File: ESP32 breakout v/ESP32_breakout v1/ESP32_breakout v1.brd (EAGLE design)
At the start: 50.8 x 50.8 mm, 18 parts, among them U1 ESP-WROOM-32, U2 AP7361C-33E-13

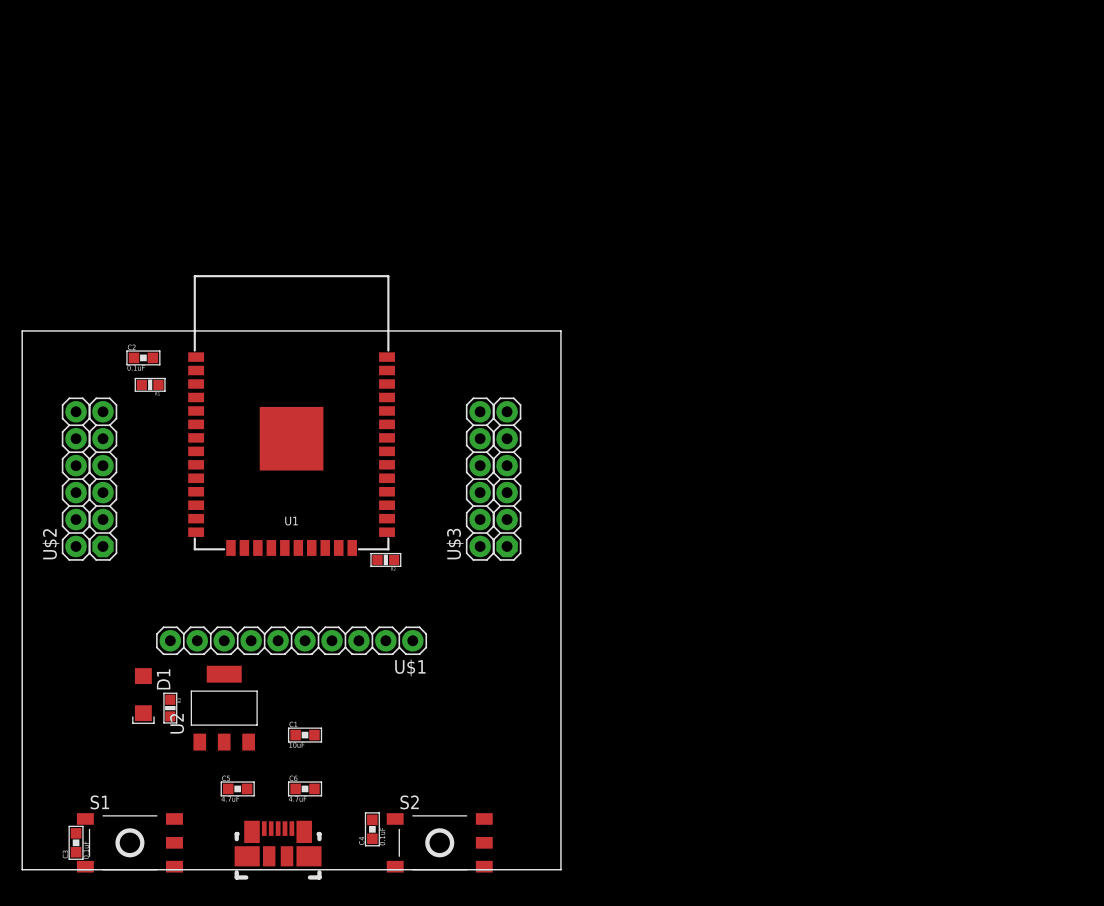
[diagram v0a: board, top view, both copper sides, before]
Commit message: Added USB ccomponents
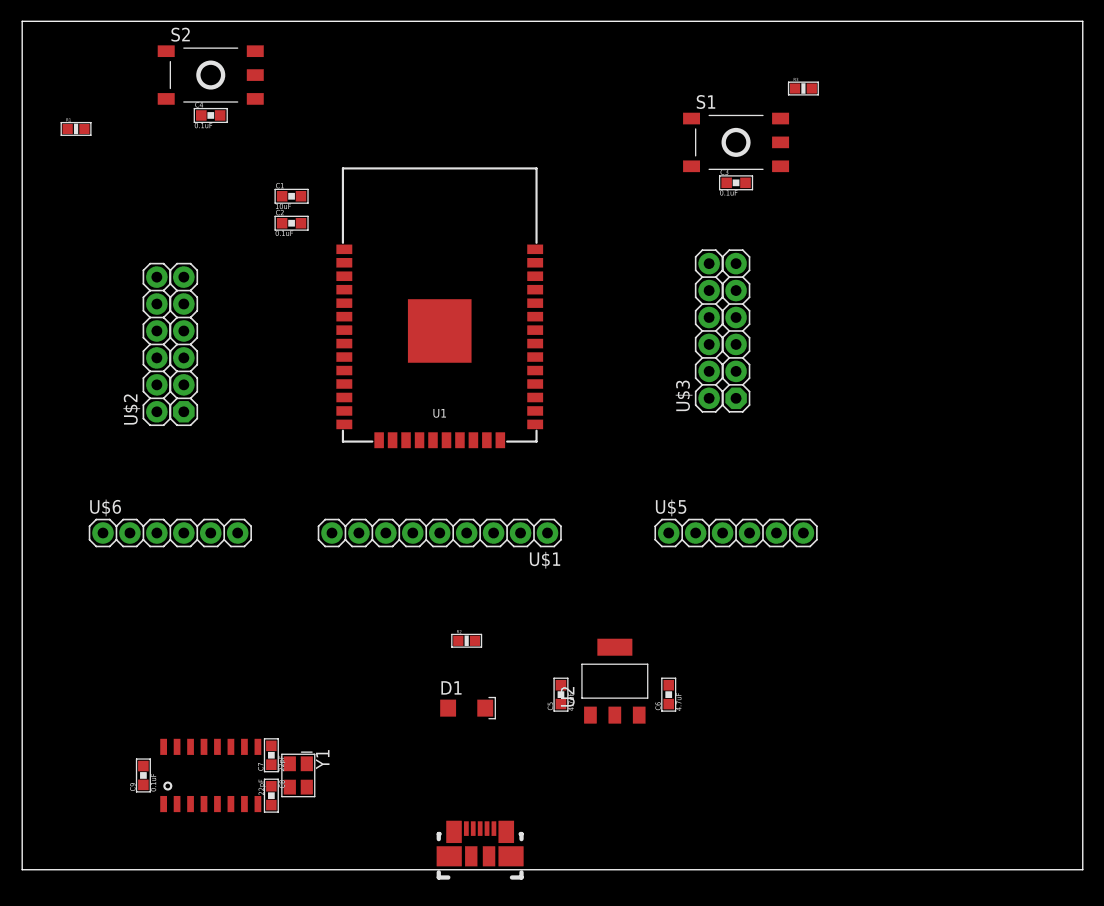
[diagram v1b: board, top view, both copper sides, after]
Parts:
- added C7, C8: 22pF, dr-library:CAP-0603
- added C9: 0.1uF, dr-library:CAP-0603
- added U$5, U$6: M06, dr-library:1X06
- added U$7: CH340G, usb-serial:SOIC16
- added Y1: (no value), dr-library:CFPX-180
- U$1: value M10 -> M09; device dr-library:1X10 -> dr-library:1X09
- moved C3 88.0 mm to (67.3, 64.8), turned to 0 degrees
- moved S1 87.3 mm to (67.3, 68.6)
- moved R3 83.5 mm to (73.7, 73.7), turned to 0 degrees
- moved S2 75.5 mm to (17.8, 74.9)
- moved C4 69.0 mm to (17.8, 71.1), turned to 0 degrees
- moved C1 50.8 mm to (25.4, 63.5)
- moved U2 36.9 mm to (55.9, 17.8)
- moved C6 35.4 mm to (61.0, 16.5), turned to 90 degrees
- moved C5 31.8 mm to (50.8, 16.5), turned to 90 degrees
- moved D1 30.5 mm to (41.9, 15.2), turned to 0 degrees
- moved U$3 25.7 mm to (64.8, 45.7)
- moved R1 25.1 mm to (5.08, 69.8), turned to 0 degrees
- moved U$4 19.1 mm to (43.2, 1.27)
- moved C2 18.9 mm to (25.4, 61.0)
- moved U1 17.3 mm to (39.4, 50.8)
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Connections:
- new net N$3: C7.1, U$7.7, Y1.1
- new net N$4: C8.1, U$7.8, Y1.3
- new net N$5: U$4.3, U$7.5
- new net N$6: U$4.2, U$7.6
- net +3V3: now also C9.2, U$7.16, U$7.4
- net CLK: now also U$1.5; no longer U$1.6
- net CMD: now also U$1.6; no longer U$1.7
- net GND: now also C7.2, C8.2, C9.1, U$7.1, Y1.2, Y1.4; no longer U$1.1
- net IO12: now also U$6.4
- net IO13: now also U$1.9, U$6.6; no longer U$1.10
- net IO14: now also U$6.5
- net IO15: now also U$1.2, U$6.1; no longer U$1.3
- net IO18: now also U$5.5
- net IO19: now also U$5.4
- net IO2: now also U$1.1, U$6.2; no longer U$1.2
- net IO21: now also U$5.3
- net IO22: now also U$5.2
- net IO23: now also U$5.6
- net IO4: now also U$6.3
- net IO5: now also U$5.1
- net RX: now also U$7.3
- net SD0: now also U$1.4; no longer U$1.5
- net SD1: now also U$1.3; no longer U$1.4
- net SD2: now also U$1.8; no longer U$1.9
- net SD3: now also U$1.7; no longer U$1.8
- net TX: now also U$7.2
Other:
- board size 50.8 x 50.8 mm -> 100 x 80 mm

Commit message: layout
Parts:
- added U$10, U$11, U$12, U$13: (no value), EmbeddedAdventures 3:STAND-OFF-HOLE
- added U$14, U$15: M05, dr-library:1X05
- added U$8: SCHA4B0419, dr-library:MICROSD_SCHA4B0419
- added U$9: M02LONG, dr-library:1X02-LONG
- C5, C6: value 4.7uF -> 10uF; device dr-library:CAP-0603 -> dr-library:B-3528
- U$1: value M09 -> M02LONG; device dr-library:1X09 -> dr-library:1X02-LONG
- U2: value AP7361C-33E-13 -> (none); device dr-library:SOT-223-3 -> dr-library:SOT-223-4
- Y1: value (none) -> 12MHz; device dr-library:CFPX-180 -> dr-library:HC-49/US
- moved R3 81.3 mm to (18.4, 14.0), turned to 270 degrees
- moved R1 71.7 mm to (40.6, 7.62), turned to 180 degrees
- moved S2 71.2 mm to (15.2, 3.81)
- moved S1 70.0 mm to (40.6, 3.81), turned to 180 degrees
- moved C4 67.8 mm to (9.53, 3.81), turned to 90 degrees
- moved C3 64.5 mm to (46.4, 3.81), turned to 270 degrees
- moved C6 57.2 mm to (3.81, 14.6)
- moved U2 47.0 mm to (8.89, 15.9)
- moved C5 36.9 mm to (14.0, 14.6)
- moved R2 30.1 mm to (15.2, 7.62), turned to 180 degrees
- moved U$5 25.7 mm to (36.8, 27.9)
- moved U$1 24.4 mm to (44.5, 55.9)
- moved Y1 23.1 mm to (48.3, 15.2), turned to 90 degrees
- moved U$3 22.5 mm to (43.2, 39.4)
- moved C7 21.9 mm to (44.5, 17.1)
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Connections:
- net +3V3: now also C6.P, U$8.4, U$9.2, U2.2, U2.PAD; no longer C6.1, U2.3
- net CLK: now also U$14.1, U$8.5; no longer U$1.5
- net CMD: now also U$15.5, U$8.3; no longer U$1.6
- net GND: now also C5.N, C6.N, U$1.1, U$15.1, U$8.6, U$8.G1, U$8.G2, U$9.1, U2.1; no longer C5.2, C6.2, U2.2, Y1.2, Y1.4
- net IO0: now also U$3.2; no longer U$3.1
- net IO13: now also U$15.2; no longer U$1.9
- net IO15: now also U$14.4; no longer U$1.2
- net IO16: now also U$3.4; no longer U$3.3
- net IO17: now also U$3.3; no longer U$3.4
- net IO18: now also U$3.5; no longer U$3.6
- net IO19: now also U$3.8; no longer U$3.7
- net IO2: now also U$14.5; no longer U$1.1
- net IO21: now also U$3.7; no longer U$3.8
- net IO22: now also U$3.12; no longer U$3.11
- net IO23: now also U$3.11; no longer U$3.12
- net IO4: now also U$3.1; no longer U$3.2
- net IO5: now also U$3.6; no longer U$3.5
- net N$3: now also Y1.P$1; no longer Y1.1
- net N$4: now also Y1.P$2; no longer Y1.3
- net RX: now also U$3.10; no longer U$3.9
- net SD0: now also U$14.2, U$8.7; no longer U$1.4
- net SD1: now also U$14.3, U$8.8; no longer U$1.3
- net SD2: now also U$15.3, U$8.1; no longer U$1.8
- net SD3: now also U$15.4, U$8.2; no longer U$1.7
- net TX: now also U$3.9; no longer U$3.10
- net VCC: now also C5.P, U$1.2, U2.3; no longer C5.1, U2.1
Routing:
- net TX: track 0.00 -> 64.7 mm
- net RX: track 0.00 -> 63.1 mm, vias 0 -> 4
- net IO22: track 0.00 -> 55.3 mm
- net IO2: track 0.00 -> 52.3 mm, vias 0 -> 1
- net IO4: track 0.00 -> 47.1 mm, vias 0 -> 1
- net IO15: track 0.00 -> 46.5 mm, vias 0 -> 1
- net IO23: track 0.00 -> 41.3 mm
- net GND: track 0.00 -> 40.7 mm
- net IO21: track 0.00 -> 38.8 mm
- net IO18: track 0.00 -> 32.8 mm
- net IO5: track 0.00 -> 29.0 mm
- net IO19: track 0.00 -> 28.0 mm
- net IO13: track 0.00 -> 26.4 mm
- net SD2: track 0.00 -> 24.8 mm, vias 0 -> 1
- net SD1: track 0.00 -> 24.7 mm, vias 0 -> 1
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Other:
- board size 100 x 80 mm -> 53.3 x 61 mm

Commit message: PCB layout
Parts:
- moved C3 25.4 mm to (21.0, 3.81)
- moved C4 25.4 mm to (34.9, 3.81)
- moved R1 25.4 mm to (15.2, 7.62)
- moved R2 25.4 mm to (40.6, 7.62)
- moved S1 25.4 mm to (15.2, 3.81)
- moved S2 25.4 mm to (40.6, 3.81)
- moved D1 2.54 mm to (20.3, 16.5)
- moved R3 1.80 mm to (17.1, 15.2)
- turned Y1 to 270 degrees
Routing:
- net +3V3: track 22.4 -> 135.1 mm, vias 0 -> 17
- net VCC: track 7.89 -> 111.9 mm, vias 0 -> 2
- net EN: track 21.2 -> 84.2 mm, vias 0 -> 1
- net GND: track 40.7 -> 95.5 mm, vias 0 -> 6
- net IO0: track 19.3 -> 68.8 mm, vias 0 -> 3
- net N$6: track 0.00 -> 17.3 mm
- net N$5: track 0.00 -> 16.7 mm
- net N$3: track 0.00 -> 12.5 mm
- net N$4: track 0.00 -> 10.00 mm
- net N$1: track 0.00 -> 4.75 mm
- added copper zone on layer 1, net +3V3
- added copper zone on layer 16, net +3V3
- added copper zone on layer 1, net GND
- added copper zone on layer 16, net GND
- added copper zone on layer 1, net VCC
- added copper zone on layer 16, net VCC

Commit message: ESP32 v1 done
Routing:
- net +3V3: track 135.1 -> 151.8 mm
- net IO12: track 20.3 -> 30.8 mm
- net IO14: track 23.4 -> 30.8 mm
- net IO4: track 47.1 -> 50.1 mm
- net IO0: track 68.8 -> 70.8 mm
- net IO15: track 46.5 -> 48.0 mm
- net GND: track 95.5 -> 96.9 mm, vias 6 -> 67
- net IO2: track 52.3 -> 53.4 mm
- net EN: track 84.2 -> 85.3 mm
- net IO5: track 29.0 -> 30.0 mm, vias 0 -> 1
- net SD1: track 24.7 -> 24.0 mm
- net SD0: track 24.1 -> 23.6 mm
- net VCC: vias 2 -> 3
- net RX: vias 4 -> 3

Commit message: Finish layout
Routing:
- net +3V3: track 151.8 -> 203.8 mm, vias 17 -> 18
- net IO15: track 48.0 -> 47.2 mm
- net GND: vias 67 -> 69
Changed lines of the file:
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@@
-<vertex x="53.34" y="0"/>
-</polygon>
-<polygon width="0.1524" layer="16" rank="2">
-<vertex x="0" y="0"/>
-<vertex x="0" y="60.96"/>
-<vertex x="53.34" y="60.96"/>
 <vertex x="53.34" y="0"/>
 </polygon>
@@
 <wire x1="29.445" y1="32.195" x2="29.945" y2="31.695" width="0.2032" layer="16"/>
 <via x="27.305" y="34.29" extent="1-16" drill="0.6"/>
+<polygon width="0.1524" layer="16" rank="2">
+<vertex x="0" y="60.96"/>
+<vertex x="0" y="0"/>
+<vertex x="53.34" y="0"/>
+<vertex x="53.34" y="60.96"/>
+<vertex x="36.83" y="60.96"/>
+<vertex x="36.83" y="58.42"/>
+<vertex x="17.78" y="58.42"/>
+<vertex x="16.51" y="58.42"/>
+<vertex x="16.51" y="60.96"/>
+</polygon>
+<via x="45.72" y="30.48" extent="1-16" drill="0.6"/>
+<via x="45.72" y="35.56" extent="1-16" drill="0.6"/>
 </signal>
 <signal name="+3V3">
@@
 <wire x1="8.615" y1="19.05" x2="8.89" y2="18.775" width="0.254" layer="1"/>
 <wire x1="10.16" y1="50.8" x2="10.16" y2="55.88" width="0.254" layer="16"/>
-<wire x1="36.83" y1="10.795" x2="39.8525" y2="7.62" width="0" layer="19" extent="1-1"/>
+<wire x1="39.8525" y1="7.62" x2="39.8525" y2="8.1025" width="0.1524" layer="1"/>
+<wire x1="39.8525" y1="8.1025" x2="40.64" y2="8.89" width="0.1524" layer="1"/>
+<wire x1="40.64" y1="8.89" x2="44.45" y2="8.89" width="0.1524" layer="1"/>
+<wire x1="44.45" y1="8.89" x2="46.99" y2="6.35" width="0.1524" layer="1"/>
+<wire x1="46.99" y1="6.35" x2="50.8" y2="6.35" width="0.1524" layer="1"/>
+<wire x1="50.8" y1="6.35" x2="52.07" y2="7.62" width="0.1524" layer="1"/>
+<wire x1="52.07" y1="7.62" x2="52.07" y2="21.59" width="0.1524" layer="1"/>
+<wire x1="52.07" y1="21.59" x2="50.8" y2="22.86" width="0.1524" layer="1"/>
+<wire x1="50.8" y1="22.86" x2="46.6725" y2="22.86" width="0.1524" layer="1"/>
+<wire x1="46.6725" y1="22.86" x2="45.72" y2="23.8125" width="0.1524" layer="1"/>
+<wire x1="45.72" y1="23.8125" x2="39.37" y2="23.8125" width="0.1524" layer="1"/>
+<via x="39.37" y="23.8125" extent="1-16" drill="0.6"/>
+<wire x1="39.37" y1="23.8125" x2="32.7025" y2="23.8125" width="0.1524" layer="16"/>
+<wire x1="32.7025" y1="23.8125" x2="30.48" y2="21.59" width="0.1524" layer="16"/>
 </signal>
 <signal name="EN">
@@
 <wire x1="31.75" y1="38.735" x2="39.0525" y2="38.735" width="0.2032" layer="1"/>
 <wire x1="39.0525" y1="38.735" x2="41.5925" y2="36.195" width="0.2032" layer="1"/>
-<wire x1="41.5925" y1="36.195" x2="45.085" y2="36.195" width="0.2032" layer="1"/>
-<wire x1="45.085" y1="36.195" x2="45.72" y2="35.56" width="0.2032" layer="1"/>
-<wire x1="45.72" y1="35.56" x2="45.72" y2="33.02" width="0.2032" layer="1"/>
+<wire x1="41.5925" y1="36.195" x2="43.815" y2="36.195" width="0.2032" layer="1"/>
+<wire x1="43.815" y1="36.195" x2="45.72" y2="34.29" width="0.2032" layer="1"/>
+<wire x1="45.72" y1="34.29" x2="45.72" y2="33.02" width="0.2032" layer="1"/>
 <wire x1="21.59" y1="29.21" x2="21.59" y2="41.275" width="0.2032" layer="16"/>
 <wire x1="21.59" y1="41.275" x2="22.86" y2="42.545" width="0.2032" layer="16"/>
